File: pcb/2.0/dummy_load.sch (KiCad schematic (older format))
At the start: 6 parts

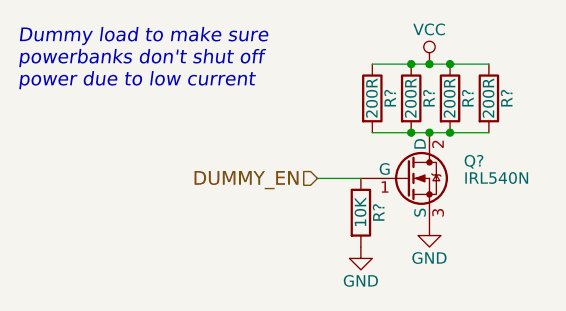
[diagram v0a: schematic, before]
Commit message: add the sound circuit
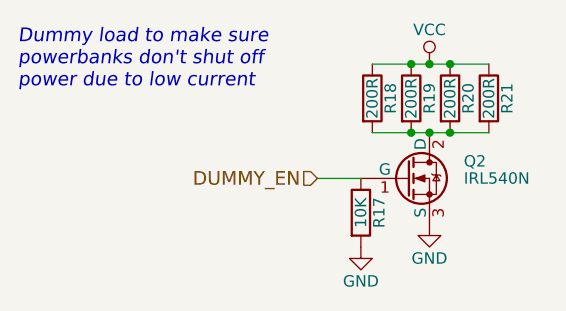
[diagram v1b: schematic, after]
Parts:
- gave numbers to parts that had none: 6
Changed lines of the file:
@@
 	5840 3660 6030 3660
 $Comp
-L R R?
+L R R18
 U 1 1 5A315BAA
 P 6080 3310
-F 0 "R?" V 6160 3310 50  0000 C CNN
+F 0 "R18" V 6160 3310 50  0000 C CNN
 F 1 "200R" V 6080 3310 50  0000 C CNN
 F 2 "" V 6010 3310 50  0001 C CNN
@@
 $EndComp
 $Comp
-L R R?
+L R R21
 U 1 1 5A315BB1
 P 6590 3310
-F 0 "R?" V 6670 3310 50  0000 C CNN
+F 0 "R21" V 6670 3310 50  0000 C CNN
 F 1 "200R" V 6590 3310 50  0000 C CNN
 F 2 "" V 6520 3310 50  0001 C CNN
@@
 $EndComp
 $Comp
-L R R?
+L R R19
 U 1 1 5A315BB8
 P 6250 3310
-F 0 "R?" V 6330 3310 50  0000 C CNN
+F 0 "R19" V 6330 3310 50  0000 C CNN
 F 1 "200R" V 6250 3310 50  0000 C CNN
 F 2 "" V 6180 3310 50  0001 C CNN
@@
 Dummy load to make sure\npowerbanks don't shut off\npower due to low current
 $Comp
-L GND #PWR?
+L GND #PWR51
 U 1 1 5A315BC0
 P 6330 3860
-F 0 "#PWR?" H 6330 3610 50  0001 C CNN
+F 0 "#PWR51" H 6330 3610 50  0001 C CNN
 F 1 "GND" H 6330 3710 50  0000 C CNN
 F 2 "" H 6330 3860 50  0001 C CNN
@@
 $EndComp
 $Comp
-L GND #PWR?
+L GND #PWR49
 U 1 1 5A315BC6
 P 6030 3960
-F 0 "#PWR?" H 6030 3710 50  0001 C CNN
+F 0 "#PWR49" H 6030 3710 50  0001 C CNN
 F 1 "GND" H 6030 3810 50  0000 C CNN
 F 2 "" H 6030 3960 50  0001 C CNN
@@
 $EndComp
 $Comp
-L R R?
+L R R17
 U 1 1 5A315BCC
 P 6030 3810
-F 0 "R?" V 6110 3810 50  0000 C CNN
+F 0 "R17" V 6110 3810 50  0000 C CNN
 F 1 "10K" V 6030 3810 50  0000 C CNN
 F 2 "" V 5960 3810 50  0001 C CNN
@@
 $EndComp
 $Comp
-L IRLIZ44N Q?
+L IRLIZ44N Q2
 U 1 1 5A315BD4
 P 6230 3660
-F 0 "Q?" H 6480 3735 50  0000 L CNN
+F 0 "Q2" H 6480 3735 50  0000 L CNN
 F 1 "IRL540N" H 6480 3660 50  0000 L CNN
 F 2 "TO_SOT_Packages_THT:TO-220-3_Horizontal" H 6480 3585 50  0001 L CIN
@@
 $EndComp
 $Comp
-L VCC #PWR?
+L VCC #PWR50
 U 1 1 5A315BDB
 P 6330 3160
-F 0 "#PWR?" H 6330 3010 50  0001 C CNN
+F 0 "#PWR50" H 6330 3010 50  0001 C CNN
 F 1 "VCC" H 6330 3310 50  0000 C CNN
 F 2 "" H 6330 3160 50  0001 C CNN
@@
 $EndComp
 $Comp
-L R R?
+L R R20
 U 1 1 5A315BE1
 P 6420 3310
-F 0 "R?" V 6500 3310 50  0000 C CNN
+F 0 "R20" V 6500 3310 50  0000 C CNN
 F 1 "200R" V 6420 3310 50  0000 C CNN
 F 2 "" V 6350 3310 50  0001 C CNN

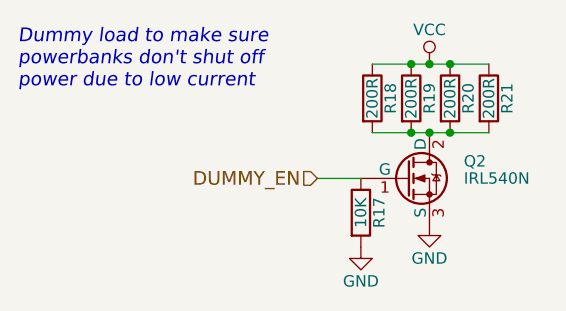
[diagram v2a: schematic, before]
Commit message: complete the 2.0 schematic
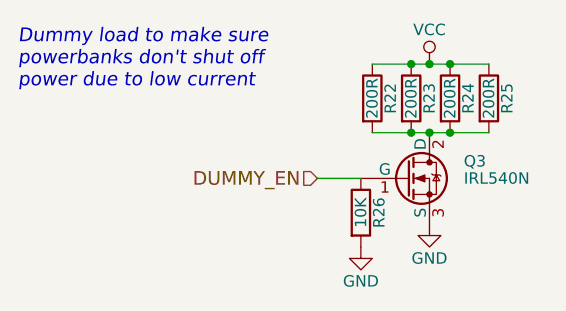
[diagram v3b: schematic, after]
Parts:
- renumbered Q2 to Q3, R18 to R22, R19 to R23, R20 to R24, R21 to R25, R17 to R26
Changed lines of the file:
@@
 	5840 3660 6030 3660
 $Comp
-L R R18
+L R R22
 U 1 1 5A315BAA
 P 6080 3310
-F 0 "R18" V 6160 3310 50  0000 C CNN
+F 0 "R22" V 6160 3310 50  0000 C CNN
 F 1 "200R" V 6080 3310 50  0000 C CNN
 F 2 "" V 6010 3310 50  0001 C CNN
@@
 $EndComp
 $Comp
-L R R21
+L R R25
 U 1 1 5A315BB1
 P 6590 3310
-F 0 "R21" V 6670 3310 50  0000 C CNN
+F 0 "R25" V 6670 3310 50  0000 C CNN
 F 1 "200R" V 6590 3310 50  0000 C CNN
 F 2 "" V 6520 3310 50  0001 C CNN
@@
 $EndComp
 $Comp
-L R R19
+L R R23
 U 1 1 5A315BB8
 P 6250 3310
-F 0 "R19" V 6330 3310 50  0000 C CNN
+F 0 "R23" V 6330 3310 50  0000 C CNN
 F 1 "200R" V 6250 3310 50  0000 C CNN
 F 2 "" V 6180 3310 50  0001 C CNN
@@
 Dummy load to make sure\npowerbanks don't shut off\npower due to low current
 $Comp
-L GND #PWR51
+L GND #PWR049
 U 1 1 5A315BC0
 P 6330 3860
-F 0 "#PWR51" H 6330 3610 50  0001 C CNN
+F 0 "#PWR049" H 6330 3610 50  0001 C CNN
 F 1 "GND" H 6330 3710 50  0000 C CNN
 F 2 "" H 6330 3860 50  0001 C CNN
@@
 $EndComp
 $Comp
-L GND #PWR49
+L GND #PWR050
 U 1 1 5A315BC6
 P 6030 3960
-F 0 "#PWR49" H 6030 3710 50  0001 C CNN
+F 0 "#PWR050" H 6030 3710 50  0001 C CNN
 F 1 "GND" H 6030 3810 50  0000 C CNN
 F 2 "" H 6030 3960 50  0001 C CNN
@@
 $EndComp
 $Comp
-L R R17
+L R R26
 U 1 1 5A315BCC
 P 6030 3810
-F 0 "R17" V 6110 3810 50  0000 C CNN
+F 0 "R26" V 6110 3810 50  0000 C CNN
 F 1 "10K" V 6030 3810 50  0000 C CNN
 F 2 "" V 5960 3810 50  0001 C CNN
@@
 $EndComp
 $Comp
-L IRLIZ44N Q2
+L IRLIZ44N Q3
 U 1 1 5A315BD4
 P 6230 3660
-F 0 "Q2" H 6480 3735 50  0000 L CNN
+F 0 "Q3" H 6480 3735 50  0000 L CNN
 F 1 "IRL540N" H 6480 3660 50  0000 L CNN
 F 2 "TO_SOT_Packages_THT:TO-220-3_Horizontal" H 6480 3585 50  0001 L CIN
@@
 $EndComp
 $Comp
-L VCC #PWR50
+L VCC #PWR051
 U 1 1 5A315BDB
 P 6330 3160
-F 0 "#PWR50" H 6330 3010 50  0001 C CNN
+F 0 "#PWR051" H 6330 3010 50  0001 C CNN
 F 1 "VCC" H 6330 3310 50  0000 C CNN
 F 2 "" H 6330 3160 50  0001 C CNN
@@
 $EndComp
 $Comp
-L R R20
+L R R24
 U 1 1 5A315BE1
 P 6420 3310
-F 0 "R20" V 6500 3310 50  0000 C CNN
+F 0 "R24" V 6500 3310 50  0000 C CNN
 F 1 "200R" V 6420 3310 50  0000 C CNN
 F 2 "" V 6350 3310 50  0001 C CNN
